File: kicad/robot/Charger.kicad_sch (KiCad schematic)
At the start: 32 parts, among them U13 MAX77976EFD+

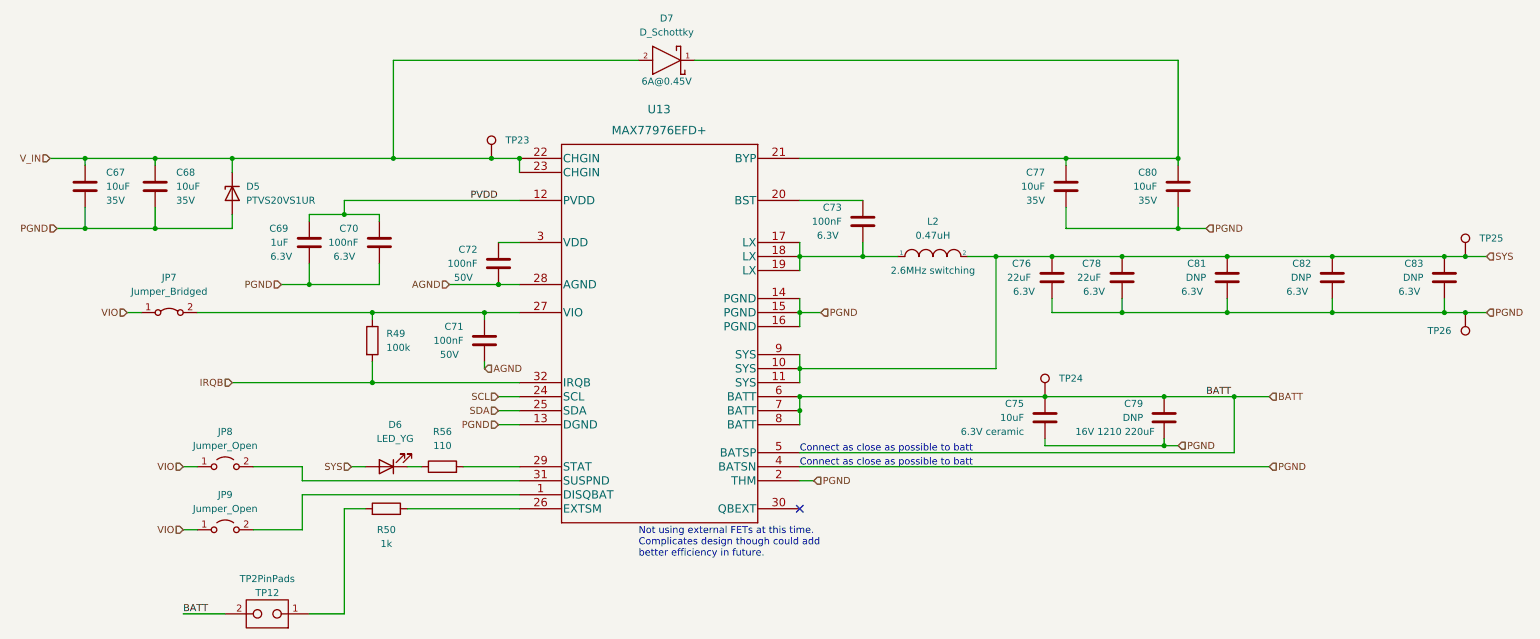
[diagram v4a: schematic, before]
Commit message: Bulk capacitor field edits
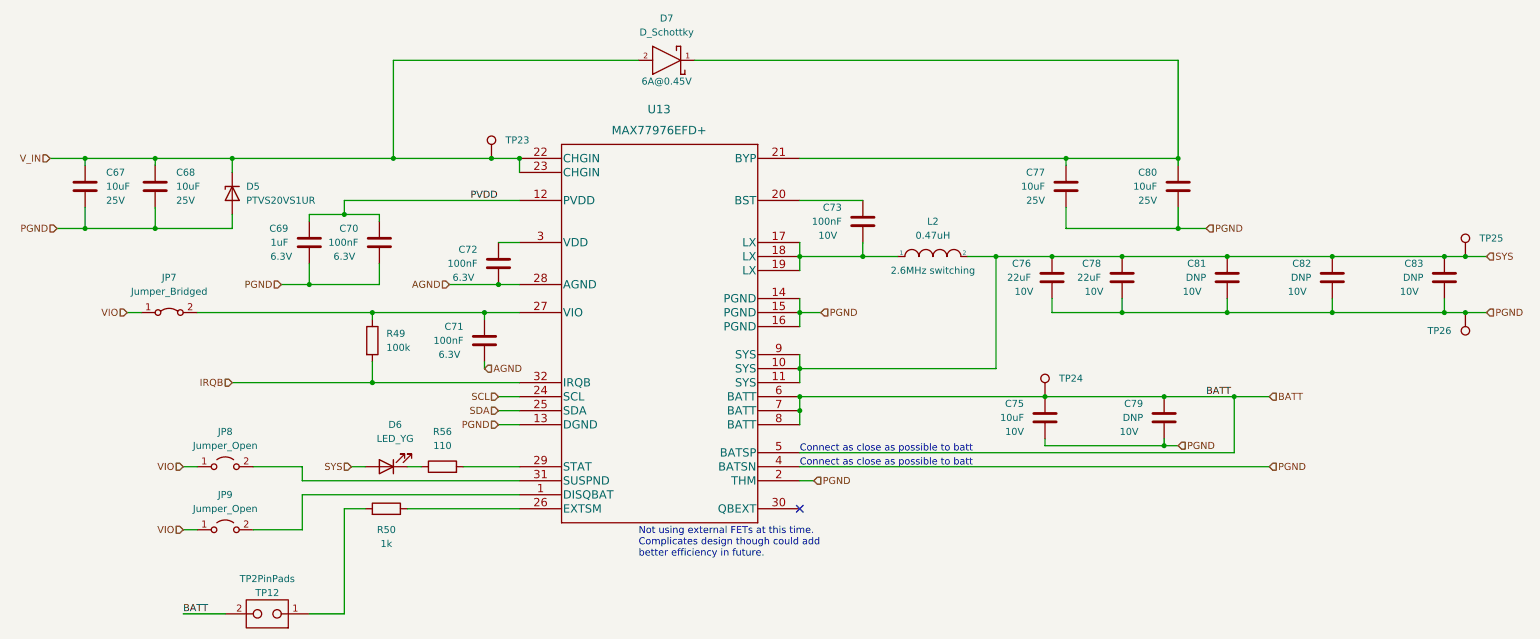
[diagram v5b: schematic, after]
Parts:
- C67, C68, C77, C80: Manufacturer Murata -> (none); Part Number GRM21BR6YA106ME43L -> (none)
- C69: Manufacturer Samsung -> (none); Part Number CL10A105KQ8NNNC -> (none)
- C71, C72: Manufacturer Samsung -> (none); Part Number CL10B104MB8NNNC -> (none)
- C75: Manufacturer Samsung -> (none); Part Number CL10A106MQ8NNNC -> (none)
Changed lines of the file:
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@@
       (effects (font (size 1.27 1.27)) hide)
     )
-    (property "Description" "6.3V ceramic" (id 4) (at 187.96 130.8099 0)
-      (effects (font (size 1.27 1.27)) (justify left))
-    )
-    (property "Manufacturer" "Samsung" (id 5) (at 191.77 128.27 0)
-      (effects (font (size 1.27 1.27)) hide)
-    )
-    (property "Part Number" "CL10A106MQ8NNNC" (id 6) (at 191.77 128.27 0)
-      (effects (font (size 1.27 1.27)) hide)
+    (property "Description" "10V" (id 4) (at 187.96 130.8099 0)
+      (effects (font (size 1.27 1.27)) (justify left))
     )
     (pin "1")
@@
       (effects (font (size 1.27 1.27)) hide)
     )
-    (property "Description" "50V" (id 4) (at 86.36 102.87 0))
-    (property "Manufacturer" "Samsung" (id 5) (at 92.71 100.33 0)
-      (effects (font (size 1.27 1.27)) hide)
-    )
-    (property "Part Number" "CL10B104MB8NNNC" (id 6) (at 92.71 100.33 0)
-      (effects (font (size 1.27 1.27)) hide)
-    )
+    (property "Description" "6.3V" (id 4) (at 86.36 102.87 0))
     (pin "1")
     (pin "2")
@@
       (effects (font (size 1.27 1.27)) hide)
     )
-    (property "Description" "50V" (id 4) (at 83.82 116.84 0))
-    (property "Manufacturer" "Samsung" (id 5) (at 90.17 114.3 0)
-      (effects (font (size 1.27 1.27)) hide)
-    )
-    (property "Part Number" "CL10B104MB8NNNC" (id 6) (at 90.17 114.3 0)
-      (effects (font (size 1.27 1.27)) hide)
-    )
+    (property "Description" "6.3V" (id 4) (at 83.82 116.84 0))
     (pin "1")
     (pin "2")
@@
       (effects (font (size 1.27 1.27)) hide)
     )
-    (property "Description" "35V" (id 4) (at 34.29 88.8999 0)
-      (effects (font (size 1.27 1.27)) (justify left))
-    )
-    (property "Manufacturer" "Murata" (id 5) (at 30.48 86.36 0)
-      (effects (font (size 1.27 1.27)) hide)
-    )
-    (property "Part Number" "GRM21BR6YA106ME43L" (id 6) (at 30.48 86.36 0)
-      (effects (font (size 1.27 1.27)) hide)
+    (property "Description" "25V" (id 4) (at 34.29 88.8999 0)
+      (effects (font (size 1.27 1.27)) (justify left))
     )
     (pin "1")
@@
       (effects (font (size 1.27 1.27)) hide)
     )
-    (property "Description" "6.3V" (id 4) (at 218.44 105.41 0))
+    (property "Description" "10V" (id 4) (at 218.44 105.41 0))
     (property "Manufacturer" "N/A" (id 5) (at 224.79 102.87 0)
       (effects (font (size 1.27 1.27)) hide)
@@
       (effects (font (size 1.27 1.27)) hide)
     )
-    (property "Description" "6.3V" (id 4) (at 237.49 105.41 0))
+    (property "Description" "10V" (id 4) (at 237.49 105.41 0))
     (property "Manufacturer" "N/A" (id 5) (at 243.84 102.87 0)
       (effects (font (size 1.27 1.27)) hide)
@@
       (effects (font (size 1.27 1.27)) hide)
     )
-    (property "Description" "6.3V" (id 4) (at 187.96 105.41 0))
+    (property "Description" "10V" (id 4) (at 187.96 105.41 0))
     (pin "1")
     (pin "2")
@@
       (effects (font (size 1.27 1.27)) hide)
     )
-    (property "Description" "6.3V" (id 4) (at 257.81 105.41 0))
+    (property "Description" "10V" (id 4) (at 257.81 105.41 0))
     (property "Manufacturer" "N/A" (id 5) (at 264.16 102.87 0)
       (effects (font (size 1.27 1.27)) hide)
@@
       (effects (font (size 1.27 1.27)) hide)
     )
-    (property "Description" "6.3V" (id 4) (at 200.66 105.41 0))
+    (property "Description" "10V" (id 4) (at 200.66 105.41 0))
     (pin "1")
     (pin "2")
@@
       (effects (font (size 1.27 1.27)) hide)
     )
-    (property "Description" "35V" (id 4) (at 21.59 88.8999 0)
-      (effects (font (size 1.27 1.27)) (justify left))
-    )
-    (property "Manufacturer" "Murata" (id 5) (at 17.78 86.36 0)
-      (effects (font (size 1.27 1.27)) hide)
-    )
-    (property "Part Number" "GRM21BR6YA106ME43L" (id 6) (at 17.78 86.36 0)
-      (effects (font (size 1.27 1.27)) hide)
+    (property "Description" "25V" (id 4) (at 21.59 88.8999 0)
+      (effects (font (size 1.27 1.27)) (justify left))
     )
     (pin "1")
@@
       (effects (font (size 1.27 1.27)) hide)
     )
-    (property "Description" "35V" (id 4) (at 212.09 88.8999 0)
-      (effects (font (size 1.27 1.27)) (justify left))
-    )
-    (property "Manufacturer" "Murata" (id 5) (at 215.9 86.36 0)
-      (effects (font (size 1.27 1.27)) hide)
-    )
-    (property "Part Number" "GRM21BR6YA106ME43L" (id 6) (at 215.9 86.36 0)
-      (effects (font (size 1.27 1.27)) hide)
+    (property "Description" "25V" (id 4) (at 212.09 88.8999 0)
+      (effects (font (size 1.27 1.27)) (justify left))
     )
     (pin "1")
@@
     )
     (property "Description" "6.3V" (id 4) (at 53.34 99.06 0))
-    (property "Manufacturer" "Samsung" (id 5) (at 58.42 96.52 0)
-      (effects (font (size 1.27 1.27)) hide)
-    )
-    (property "Part Number" "CL10A105KQ8NNNC" (id 6) (at 58.42 96.52 0)
-      (effects (font (size 1.27 1.27)) hide)
-    )
     (pin "1")
     (pin "2")
@@
       (effects (font (size 1.27 1.27)) hide)
     )
-    (property "Description" "35V" (id 4) (at 191.77 88.8999 0)
-      (effects (font (size 1.27 1.27)) (justify left))
-    )
-    (property "Manufacturer" "Murata" (id 5) (at 195.58 86.36 0)
-      (effects (font (size 1.27 1.27)) hide)
-    )
-    (property "Part Number" "GRM21BR6YA106ME43L" (id 6) (at 195.58 86.36 0)
-      (effects (font (size 1.27 1.27)) hide)
+    (property "Description" "25V" (id 4) (at 191.77 88.8999 0)
+      (effects (font (size 1.27 1.27)) (justify left))
     )
     (pin "1")
@@
       (effects (font (size 1.27 1.27)) hide)
     )
-    (property "Description" "16V 1210 220uF" (id 4) (at 204.47 130.81 0))
+    (property "Description" "10V" (id 4) (at 207.01 130.81 0))
     (property "Manufacturer" "N/A" (id 5) (at 213.36 128.27 0)
       (effects (font (size 1.27 1.27)) hide)
@@
       (effects (font (size 1.27 1.27)) hide)
     )
-    (property "Description" "6.3V" (id 4) (at 152.4 95.25 0))
-    (pin "1")
-    (pin "2")
+    (property "Description" "10V" (id 4) (at 152.4 95.25 0))
+    (pin "1")
+    (pin "2")

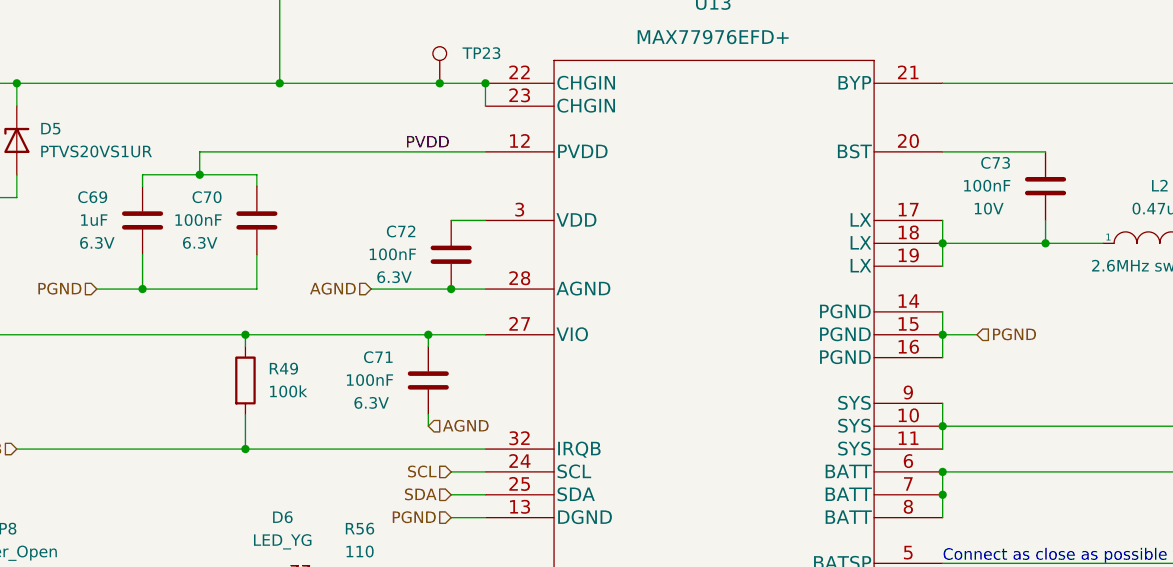
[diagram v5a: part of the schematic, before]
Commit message: bulk footprint updates to capacitors
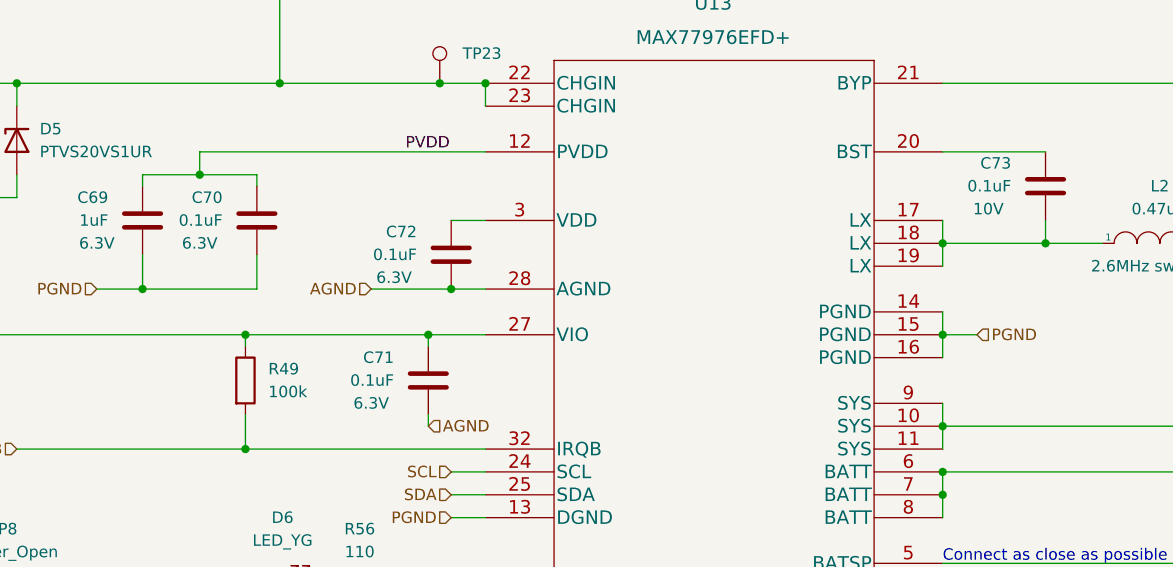
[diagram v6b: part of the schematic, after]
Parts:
- C67, C68, C76, C77, C78, C80: footprint Capacitor_SMD:C_0805_2012Metric -> Capacitor_SMD:C_0603_1608Metric
- C69: footprint Capacitor_SMD:C_0603_1608Metric -> Capacitor_SMD:C_0402_1005Metric
- C70, C71, C72, C73: value 100nF -> 0.1uF; footprint Capacitor_SMD:C_0603_1608Metric -> Capacitor_SMD:C_0402_1005Metric
- C79: footprint Capacitor_SMD:C_1210_3225Metric -> Capacitor_SMD:C_0805_2012Metric
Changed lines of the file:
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@@
       (effects (font (size 1.27 1.27)) (justify left))
     )
-    (property "Value" "100nF" (id 1) (at 88.9 100.3299 0)
-      (effects (font (size 1.27 1.27)) (justify left))
-    )
-    (property "Footprint" "Capacitor_SMD:C_0603_1608Metric" (id 2) (at 91.7448 104.14 0)
+    (property "Value" "0.1uF" (id 1) (at 88.9 100.3299 0)
+      (effects (font (size 1.27 1.27)) (justify left))
+    )
+    (property "Footprint" "Capacitor_SMD:C_0402_1005Metric" (id 2) (at 91.7448 104.14 0)
       (effects (font (size 1.27 1.27)) hide)
     )
@@
       (effects (font (size 1.27 1.27)) (justify left))
     )
-    (property "Value" "100nF" (id 1) (at 86.36 114.2999 0)
-      (effects (font (size 1.27 1.27)) (justify left))
-    )
-    (property "Footprint" "Capacitor_SMD:C_0603_1608Metric" (id 2) (at 89.2048 118.11 0)
+    (property "Value" "0.1uF" (id 1) (at 86.36 114.2999 0)
+      (effects (font (size 1.27 1.27)) (justify left))
+    )
+    (property "Footprint" "Capacitor_SMD:C_0402_1005Metric" (id 2) (at 89.2048 118.11 0)
       (effects (font (size 1.27 1.27)) hide)
     )
@@
       (effects (font (size 1.27 1.27)) (justify left))
     )
-    (property "Footprint" "Capacitor_SMD:C_0805_2012Metric" (id 2) (at 31.4452 90.17 0)
+    (property "Footprint" "Capacitor_SMD:C_0603_1608Metric" (id 2) (at 31.4452 90.17 0)
       (effects (font (size 1.27 1.27)) hide)
     )
@@
       (effects (font (size 1.27 1.27)) (justify left))
     )
-    (property "Value" "100nF" (id 1) (at 67.31 96.5199 0)
-      (effects (font (size 1.27 1.27)) (justify left))
-    )
-    (property "Footprint" "Capacitor_SMD:C_0603_1608Metric" (id 2) (at 70.1548 100.33 0)
+    (property "Value" "0.1uF" (id 1) (at 67.31 96.5199 0)
+      (effects (font (size 1.27 1.27)) (justify left))
+    )
+    (property "Footprint" "Capacitor_SMD:C_0402_1005Metric" (id 2) (at 70.1548 100.33 0)
       (effects (font (size 1.27 1.27)) hide)
     )
@@
       (effects (font (size 1.27 1.27)) (justify left))
     )
-    (property "Footprint" "Capacitor_SMD:C_0805_2012Metric" (id 2) (at 192.0748 106.68 0)
+    (property "Footprint" "Capacitor_SMD:C_0603_1608Metric" (id 2) (at 192.0748 106.68 0)
       (effects (font (size 1.27 1.27)) hide)
     )
@@
       (effects (font (size 1.27 1.27)) (justify left))
     )
-    (property "Footprint" "Capacitor_SMD:C_0805_2012Metric" (id 2) (at 204.7748 106.68 0)
+    (property "Footprint" "Capacitor_SMD:C_0603_1608Metric" (id 2) (at 204.7748 106.68 0)
       (effects (font (size 1.27 1.27)) hide)
     )
@@
       (effects (font (size 1.27 1.27)) (justify left))
     )
-    (property "Footprint" "Capacitor_SMD:C_0805_2012Metric" (id 2) (at 18.7452 90.17 0)
+    (property "Footprint" "Capacitor_SMD:C_0603_1608Metric" (id 2) (at 18.7452 90.17 0)
       (effects (font (size 1.27 1.27)) hide)
     )
@@
       (effects (font (size 1.27 1.27)) (justify left))
     )
-    (property "Footprint" "Capacitor_SMD:C_0805_2012Metric" (id 2) (at 214.9348 90.17 0)
+    (property "Footprint" "Capacitor_SMD:C_0603_1608Metric" (id 2) (at 214.9348 90.17 0)
       (effects (font (size 1.27 1.27)) hide)
     )
@@
       (effects (font (size 1.27 1.27)) (justify left))
     )
-    (property "Footprint" "Capacitor_SMD:C_0603_1608Metric" (id 2) (at 57.4548 100.33 0)
+    (property "Footprint" "Capacitor_SMD:C_0402_1005Metric" (id 2) (at 57.4548 100.33 0)
       (effects (font (size 1.27 1.27)) hide)
     )
@@
       (effects (font (size 1.27 1.27)) (justify left))
     )
-    (property "Footprint" "Capacitor_SMD:C_0805_2012Metric" (id 2) (at 194.6148 90.17 0)
+    (property "Footprint" "Capacitor_SMD:C_0603_1608Metric" (id 2) (at 194.6148 90.17 0)
       (effects (font (size 1.27 1.27)) hide)
     )
@@
       (effects (font (size 1.27 1.27)) (justify left))
     )
-    (property "Footprint" "Capacitor_SMD:C_1210_3225Metric" (id 2) (at 212.3948 132.08 0)
+    (property "Footprint" "Capacitor_SMD:C_0805_2012Metric" (id 2) (at 212.3948 132.08 0)
       (effects (font (size 1.27 1.27)) hide)
     )
@@
       (effects (font (size 1.27 1.27)) (justify left))
     )
-    (property "Value" "100nF" (id 1) (at 154.94 92.7099 0)
-      (effects (font (size 1.27 1.27)) (justify left))
-    )
-    (property "Footprint" "Capacitor_SMD:C_0603_1608Metric" (id 2) (at 157.7848 96.52 0)
-      (effects (font (size 1.27 1.27)) hide)
-    )
+    (property "Value" "0.1uF" (id 1) (at 154.94 92.7099 0)
+      (effects (font (size 1.27 1.27)) (justify left))
+    )
+    (property "Footprint" "Capacitor_SMD:C_0402_1005Metric" (id 2) (at 157.7848 96.52 0)
+      (effects (font (size 1.27 1.27)) hide)
+    )

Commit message: Bulk BOM edits and one replaced footprint for U15
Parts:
- C67, C68, C75, C77, C80: Manufacturer (none) -> Murata; Part Number (none) -> GRM188R61E106KA73J
- C69: Manufacturer (none) -> Murata; Part Number (none) -> GRM155R61E105KA12D
- C70, C71, C72, C73: Manufacturer (none) -> Samsung; Part Number (none) -> CL05A104KA5NNNC
- C76, C78: Manufacturer (none) -> Murata; Part Number (none) -> GRM188R61A226ME15D
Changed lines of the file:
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@@
       (effects (font (size 1.27 1.27)) (justify left))
+    )
+    (property "Manufacturer" "Murata" (id 5) (at 191.77 128.27 0)
+      (effects (font (size 1.27 1.27)) hide)
+    )
+    (property "Part Number" "GRM188R61E106KA73J" (id 6) (at 191.77 128.27 0)
+      (effects (font (size 1.27 1.27)) hide)
     )
     (pin "1")
@@
     )
     (property "Description" "6.3V" (id 4) (at 86.36 102.87 0))
+    (property "Manufacturer" "Samsung" (id 5) (at 92.71 100.33 0)
+      (effects (font (size 1.27 1.27)) hide)
+    )
+    (property "Part Number" "CL05A104KA5NNNC" (id 6) (at 92.71 100.33 0)
+      (effects (font (size 1.27 1.27)) hide)
+    )
     (pin "1")
     (pin "2")
@@
     )
     (property "Description" "6.3V" (id 4) (at 83.82 116.84 0))
+    (property "Manufacturer" "Samsung" (id 5) (at 90.17 114.3 0)
+      (effects (font (size 1.27 1.27)) hide)
+    )
+    (property "Part Number" "CL05A104KA5NNNC" (id 6) (at 90.17 114.3 0)
+      (effects (font (size 1.27 1.27)) hide)
+    )
     (pin "1")
     (pin "2")
@@
     (property "Description" "25V" (id 4) (at 34.29 88.8999 0)
       (effects (font (size 1.27 1.27)) (justify left))
+    )
+    (property "Manufacturer" "Murata" (id 5) (at 30.48 86.36 0)
+      (effects (font (size 1.27 1.27)) hide)
+    )
+    (property "Part Number" "GRM188R61E106KA73J" (id 6) (at 30.48 86.36 0)
+      (effects (font (size 1.27 1.27)) hide)
     )
     (pin "1")
@@
     )
     (property "Description" "6.3V" (id 4) (at 64.77 99.06 0))
+    (property "Manufacturer" "Samsung" (id 5) (at 71.12 96.52 0)
+      (effects (font (size 1.27 1.27)) hide)
+    )
+    (property "Part Number" "CL05A104KA5NNNC" (id 6) (at 71.12 96.52 0)
+      (effects (font (size 1.27 1.27)) hide)
+    )
     (pin "1")
     (pin "2")
@@
     )
     (property "Description" "10V" (id 4) (at 187.96 105.41 0))
+    (property "Manufacturer" "Murata" (id 5) (at 193.04 102.87 0)
+      (effects (font (size 1.27 1.27)) hide)
+    )
+    (property "Part Number" "GRM188R61A226ME15D" (id 6) (at 193.04 102.87 0)
+      (effects (font (size 1.27 1.27)) hide)
+    )
     (pin "1")
     (pin "2")
@@
     )
     (property "Description" "10V" (id 4) (at 200.66 105.41 0))
+    (property "Manufacturer" "Murata" (id 5) (at 205.74 102.87 0)
+      (effects (font (size 1.27 1.27)) hide)
+    )
+    (property "Part Number" "GRM188R61A226ME15D" (id 6) (at 205.74 102.87 0)
+      (effects (font (size 1.27 1.27)) hide)
+    )
     (pin "1")
     (pin "2")
@@
       (effects (font (size 1.27 1.27)) (justify left))
     )
+    (property "Manufacturer" "Murata" (id 5) (at 17.78 86.36 0)
+      (effects (font (size 1.27 1.27)) hide)
+    )
+    (property "Part Number" "GRM188R61E106KA73J" (id 6) (at 17.78 86.36 0)
+      (effects (font (size 1.27 1.27)) hide)
+    )
     (pin "1")
     (pin "2")
@@
       (effects (font (size 1.27 1.27)) (justify left))
     )
+    (property "Manufacturer" "Murata" (id 5) (at 215.9 86.36 0)
+      (effects (font (size 1.27 1.27)) hide)
+    )
+    (property "Part Number" "GRM188R61E106KA73J" (id 6) (at 215.9 86.36 0)
+      (effects (font (size 1.27 1.27)) hide)
+    )
     (pin "1")
     (pin "2")
@@
     )
     (property "Description" "6.3V" (id 4) (at 53.34 99.06 0))
+    (property "Manufacturer" "Murata" (id 5) (at 58.42 96.52 0)
+      (effects (font (size 1.27 1.27)) hide)
+    )
+    (property "Part Number" "GRM155R61E105KA12D" (id 6) (at 58.42 96.52 0)
+      (effects (font (size 1.27 1.27)) hide)
+    )
     (pin "1")
     (pin "2")
@@
       (effects (font (size 1.27 1.27)) (justify left))
     )
+    (property "Manufacturer" "Murata" (id 5) (at 195.58 86.36 0)
+      (effects (font (size 1.27 1.27)) hide)
+    )
+    (property "Part Number" "GRM188R61E106KA73J" (id 6) (at 195.58 86.36 0)
+      (effects (font (size 1.27 1.27)) hide)
+    )
     (pin "1")
     (pin "2")
@@
     )
     (property "Description" "10V" (id 4) (at 152.4 95.25 0))
-    (pin "1")
-    (pin "2")
+    (property "Manufacturer" "Samsung" (id 5) (at 158.75 92.71 0)
+      (effects (font (size 1.27 1.27)) hide)
+    )
+    (property "Part Number" "CL05A104KA5NNNC" (id 6) (at 158.75 92.71 0)
+      (effects (font (size 1.27 1.27)) hide)
+    )
+    (pin "1")
+    (pin "2")
